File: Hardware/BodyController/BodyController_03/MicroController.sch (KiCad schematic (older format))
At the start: 17 parts, among them U1 PIC33EPxxxMU810, Y1 8MHz

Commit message: started serious layout
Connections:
- net FAN_SPEED_2_PWM is gone; now on net PUMP_SPEED_1_PWM: U1.88 (VCMPST2/RP97/RF1)
- net PUMP_SPEED_2_PWM is gone; now on net FAN_1_EN: U1.51 (USBID/RP99/RF3)
- net BATT_~FAULT: now also U1.19 (AN21/RPI89/RE9); no longer U1.5 (AN31/PWM4H/PMD7/RP87/RE7)
- net FAN_1_EN: no longer U1.53 (RP104/RF8)
- net IC_CONTROLLER_SLEEP: no longer U1.59 (ASDA2/RPI19/RA3)
- net IC_CONTROLLER_~FLT: now also U1.5 (AN31/PWM4H/PMD7/RP87/RE7); no longer U1.19 (AN21/RPI89/RE9)
- net PUMP_1_EN: now also U1.52 (RP98/RF2); no longer U1.49 (SDA2/PMA9/RP100/RF4)
- net PUMP_SPEED_1_PWM: no longer U1.52 (RP98/RF2)
- net BRAKE_SWITCH_2_IN: now reaches U1.40 (RP108/RF12)
- net TURN_RIGHT_SWITCH_IN: now reaches U1.56 (D-/RG3)
- net TURN_LEFT_SWITCH_IN: now reaches U1.57 (D+/RG2)
- net SPARE_SWITCH_1_IN: now reaches U1.7 (AN17/PWM5H/RPI50/RC2)
- net SPARE_SWITCH_2_IN: now reaches U1.8 (AN18/PWM6L/RPI51/RC3)
- net KILL_SWITCH_IN: now reaches U1.89 (RP113/RG1)
- net IGNITION_SWITCH_IN: now reaches U1.90 (RP112/RG0)
- net KICKSTAND_SWITCH_IN: now reaches U1.95 (RP126/RG14)
- net BRIGHTS_SWITCH_IN: now reaches U1.96 (RPI124/RG12)
- net HORN_SWITCH_IN: now reaches U1.97 (RP125/RG13)
- net 12P_MONITOR renamed 12P_MONITOR_AI
- net 12V_MONITOR renamed 12V_MONITOR_AI
- net AUX_PORT_ISENSE renamed AUX_PORT_ISENSE_AI
- net BATT_ISENSE renamed BATT_ISENSE_AI
- net DCDC_ISENSE renamed DCDC_ISENSE_AI
- net ECU_1_ISENSE renamed ECU_1_ISENSE_AI
- net ECU_2_ISENSE renamed ECU_2_ISENSE_AI
- net FAN_2_EN renamed BRAKE_SWITCH_1_IN
- net FAN_ISENSE renamed FAN_ISENSE_AI
- net HEADLIGHT_ISENSE renamed HEADLIGHT_ISENSE_AI
- net HEATER_ISENSE renamed HEATER_ISENSE_AI
- net HORN_ISENSE renamed HORN_ISENSE_AI
- net IC_CONTROLLER_ISENSE renamed IC_CONTROLLER_ISENSE_AI
- net LOCK_ISENSE renamed LOCK_ISENSE_AI
- net PUMP_2_EN renamed DAC_PWM_2
- net PUMP_ISENSE renamed THROTTLE_SIGNAL_MONITOR_AI
- net TAILLIGHT_ISENSE renamed TAILLIGHT_ISENSE_AI
- new net DAC_PWM_1: U1.49 (SDA2/PMA9/RP100/RF4)
- no-connect marks 1 -> 6
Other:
- moved on the sheet: C1, C2, C3, C37, C4, C5, C6, C61, C7, C8, C9, L1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

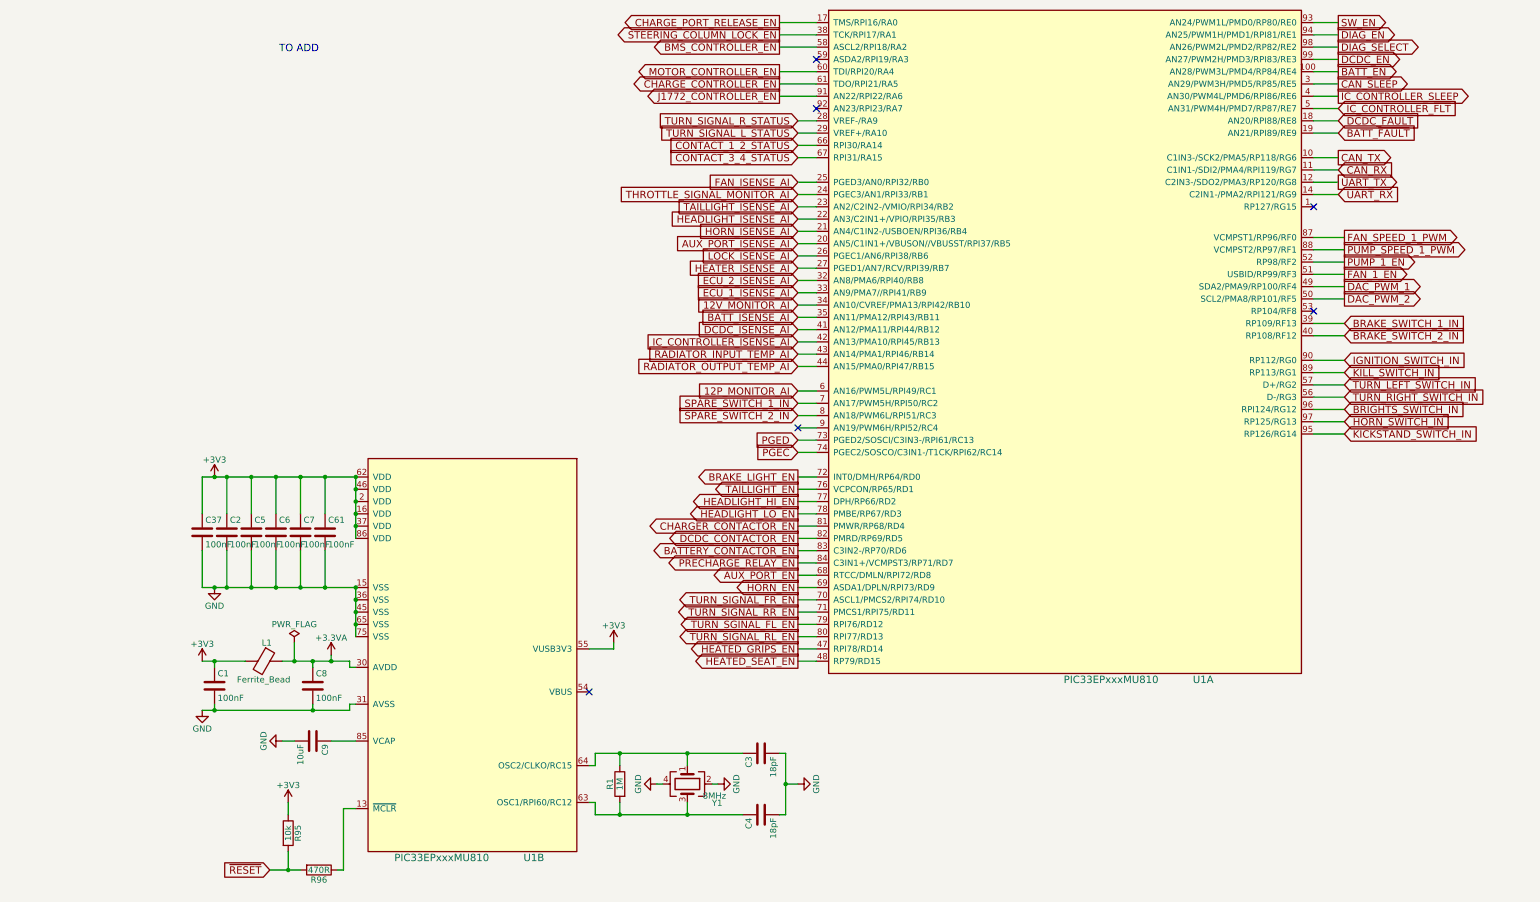
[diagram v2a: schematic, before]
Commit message: Body Controller Layout Done
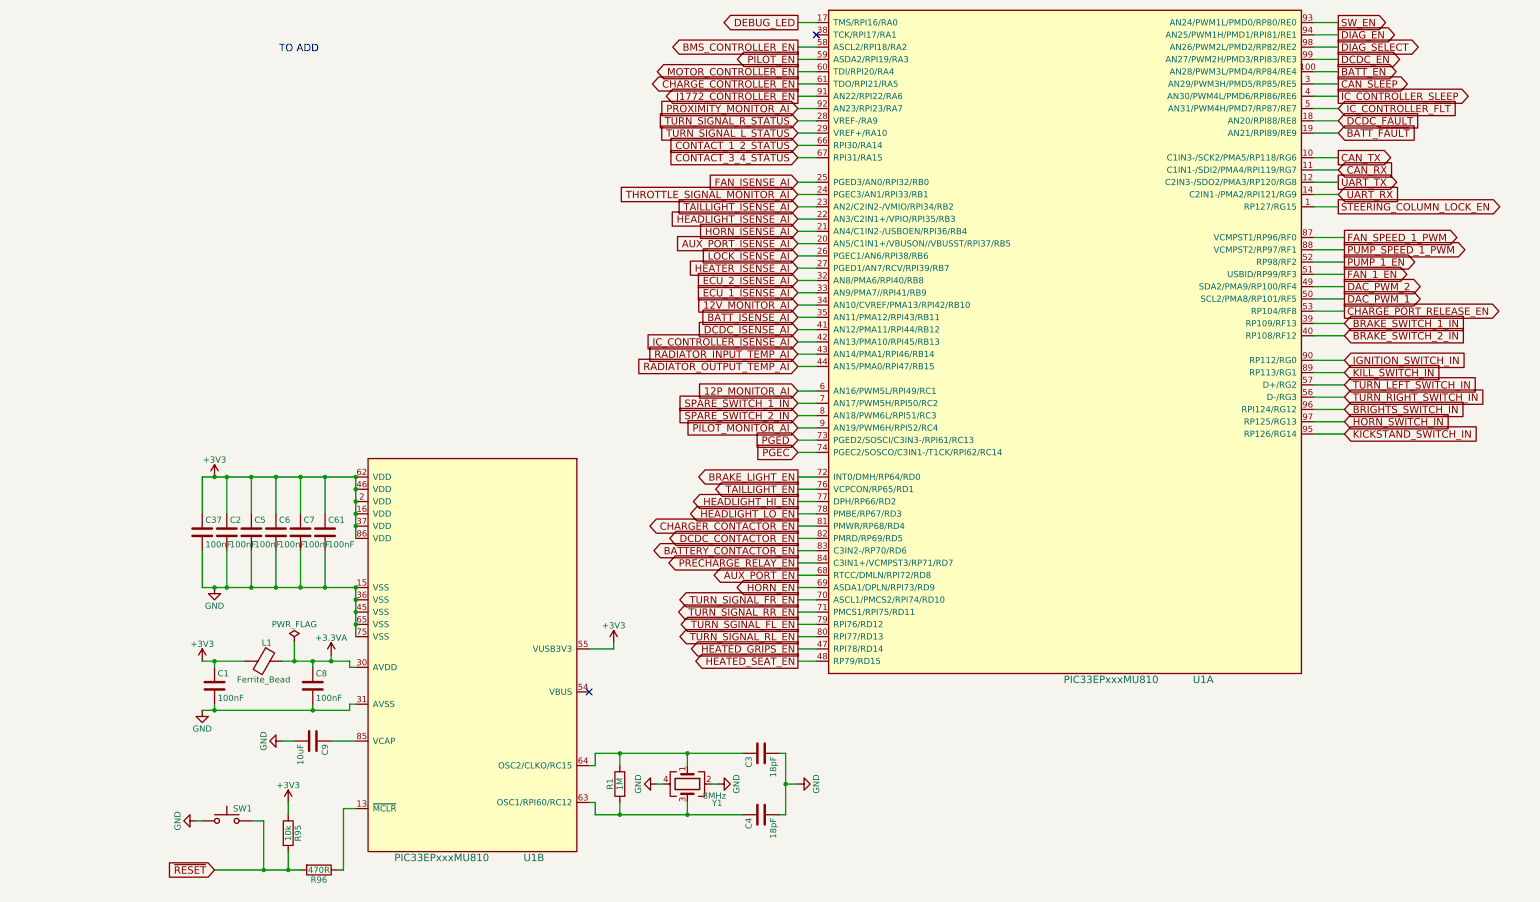
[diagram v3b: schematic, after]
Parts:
- added SW1: PTS645SM43SMTR92 LFS, Buttons_Switches_SMD:SW_SPST_EVQP0, symbol SW_Push
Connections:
- net CHARGE_PORT_RELEASE_EN: now also U1.53 (RP104/RF8); no longer U1.17 (TMS/RPI16/RA0)
- net DAC_PWM_1: now also U1.50 (SCL2/PMA8/RP101/RF5); no longer U1.49 (SDA2/PMA9/RP100/RF4)
- net DAC_PWM_2: now also U1.49 (SDA2/PMA9/RP100/RF4); no longer U1.50 (SCL2/PMA8/RP101/RF5)
- net GND: now also SW1.1
- net STEERING_COLUMN_LOCK_EN: now also U1.1 (RP127/RG15); no longer U1.38 (TCK/RPI17/RA1)
- net ~RESET: now also SW1.2
- net PILOT_EN: now reaches U1.59 (ASDA2/RPI19/RA3)
- net PILOT_MONITOR_AI: now reaches U1.9 (AN19/PWM6H/RPI52/RC4)
- net PROXIMITY_MONITOR_AI: now reaches U1.92 (AN23/RPI23/RA7)
- new net DEBUG_LED: U1.17 (TMS/RPI16/RA0)
- no-connect marks 6 -> 2
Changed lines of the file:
@@
 LIBS:ICs
 LIBS:Connectors
+LIBS:microchip_dspic33dsc
+LIBS:switches
 LIBS:BodyController_03-cache
 EELAYER 25 0
@@
 $Descr A4 11693 8268
 encoding utf-8
-Sheet 3 12
+Sheet 3 13
 Title ""
 Date ""
@@
 	1    4450 6900
 	0    1    -1   0
+$EndComp
+$Comp
+L GND #PWR013
+U 1 1 5A45E91E
+P 700 7200
+F 0 "#PWR013" H 700 6950 50  0001 C CNN
+F 1 "GND" H 700 7050 50  0000 C CNN
+F 2 "" H 700 7200 50  0001 C CNN
+F 3 "" H 700 7200 50  0001 C CNN
+	1    700  7200
+	0    1    1    0
+$EndComp
+$Comp
+L SW_Push SW1
+U 1 1 5A45E5E7
+P 950 7200
+F 0 "SW1" H 1000 7300 50  0000 L CNN
+F 1 "PTS645SM43SMTR92 LFS" H 950 7140 50  0001 C CNN
+F 2 "Buttons_Switches_SMD:SW_SPST_EVQP0" H 950 7400 50  0001 C CNN
+F 3 "https://www.ckswitches.com/media/1471/pts645.pdf" H 950 7400 50  0001 C CNN
+F 4 "PTS645SM43SMTR92 LFS" H 0   0   50  0001 C CNN "PartNumber"
+	1    950  7200
+	1    0    0    -1
 $EndComp
 Text GLabel 10000 700  2    59   Output ~ 0
@@
 Text GLabel 5600 3400 0    60   Input ~ 0
 RADIATOR_INPUT_TEMP_AI
-Text GLabel 5450 700  0    59   Output ~ 0
+Text GLabel 10050 3050 2    59   Output ~ 0
 CHARGE_PORT_RELEASE_EN
-Text GLabel 5450 800  0    59   Output ~ 0
+Text GLabel 10000 2200 2    59   Output ~ 0
 STEERING_COLUMN_LOCK_EN
 Text GLabel 5600 2600 0    59   Input ~ 0
@@
 Text GLabel 5600 1800 0    59   Input ~ 0
 CONTACT_3_4_STATUS
-Text GLabel 5450 1100 0    59   Output ~ 0
+Text GLabel 5600 1100 0    59   Output ~ 0
 MOTOR_CONTROLLER_EN
-Text GLabel 5450 1200 0    59   Output ~ 0
+Text GLabel 5600 1200 0    59   Output ~ 0
 CHARGE_CONTROLLER_EN
 Text GLabel 5600 2800 0    59   Input ~ 0
 ECU_2_ISENSE_AI
-Text GLabel 5450 900  0    59   Output ~ 0
+Text GLabel 5600 900  0    59   Output ~ 0
 BMS_CONTROLLER_EN
 Text GLabel 5600 2900 0    59   Input ~ 0
@@
 Text Notes 1700 950  2    60   ~ 0
 TO ADD
-Text GLabel 1300 7600 0    60   Input ~ 0
+Text GLabel 850  7600 0    60   Input ~ 0
 ~RESET
 Text GLabel 5600 4100 0    60   Input ~ 0
@@
 Text GLabel 10000 1300 2    59   Output ~ 0
 IC_CONTROLLER_SLEEP
-Text GLabel 5450 1300 0    59   Output ~ 0
+Text GLabel 5600 1300 0    59   Output ~ 0
 J1772_CONTROLLER_EN
 Text GLabel 10050 2450 2    60   Output ~ 0
@@
 Text GLabel 5600 3900 0    60   Input ~ 0
 SPARE_SWITCH_2_IN
+Text GLabel 5600 2100 0    60   Input ~ 0
+THROTTLE_SIGNAL_MONITOR_AI
+Text GLabel 10050 3150 2    60   Input ~ 0
+BRAKE_SWITCH_1_IN
+Text GLabel 10050 3250 2    60   Input ~ 0
+BRAKE_SWITCH_2_IN
+Text GLabel 10050 2950 2    60   Output ~ 0
+DAC_PWM_1
+Text GLabel 10050 2850 2    60   Output ~ 0
+DAC_PWM_2
+Text GLabel 5600 700  0    60   Output ~ 0
+DEBUG_LED
+Text GLabel 5600 4000 0    60   Input ~ 0
+PILOT_MONITOR_AI
+Text GLabel 5600 1400 0    60   Input ~ 0
+PROXIMITY_MONITOR_AI
+Text GLabel 5600 1000 0    60   Output ~ 0
+PILOT_EN
 Wire Wire Line
 	750  5300 2000 5300
@@
 	1450 7050 1450 7150
 Wire Wire Line
-	1450 7450 1450 7600
-Wire Wire Line
-	1300 7600 1550 7600
+	1450 7600 1450 7450
+Wire Wire Line
+	850  7600 1550 7600
 Wire Wire Line
 	1800 5850 1800 5900
@@
 	5600 1500 5750 1500
 Wire Wire Line
-	5750 1300 5450 1300
-Wire Wire Line
-	5450 1200 5750 1200
-Wire Wire Line
-	5750 1100 5450 1100
-Wire Wire Line
-	5750 900  5450 900
-Wire Wire Line
-	5450 800  5750 800
-Wire Wire Line
-	5750 700  5450 700
+	5750 1300 5600 1300
+Wire Wire Line
+	5600 1200 5750 1200
+Wire Wire Line
+	5750 1100 5600 1100
+Wire Wire Line
+	5750 900  5600 900
+Wire Wire Line
+	5750 700  5600 700
 Wire Wire Line
 	4100 5750 4100 5800
@@
 Wire Wire Line
 	5750 3900 5600 3900
+Wire Wire Line
+	5600 4000 5750 4000
+Wire Wire Line
+	10050 3250 9800 3250
+Wire Wire Line
+	10050 2950 9800 2950
+Wire Wire Line
+	9800 2850 10050 2850
+Wire Wire Line
+	5750 2100 5600 2100
+Wire Wire Line
+	9800 2200 10000 2200
+Wire Wire Line
+	1250 7600 1250 7200
+Wire Wire Line
+	750  7200 700  7200
+Wire Wire Line
+	1250 7200 1150 7200
+Wire Wire Line
+	10050 3050 9800 3050
+Wire Wire Line
+	5750 1400 5600 1400
+Wire Wire Line
+	5750 1000 5600 1000
 Connection ~ 950  4400
 Connection ~ 1150 4400
@@
 Connection ~ 5500 6900
 Connection ~ 2000 4400
+Connection ~ 1250 7600
 NoConn ~ 3900 6150
-Text GLabel 5600 2100 0    60   Input ~ 0
-THROTTLE_SIGNAL_MONITOR_AI
-Text GLabel 10050 3150 2    60   Input ~ 0
-BRAKE_SWITCH_1_IN
-Text GLabel 10050 3250 2    60   Input ~ 0
-BRAKE_SWITCH_2_IN
-Wire Wire Line
-	5600 4000 5750 4000
-Wire Wire Line
-	10050 3250 9800 3250
-NoConn ~ 9800 3050
-NoConn ~ 9800 2200
-NoConn ~ 5750 1000
-NoConn ~ 5750 1400
-Text GLabel 10050 2850 2    60   Output ~ 0
-DAC_PWM_1
-Text GLabel 10050 2950 2    60   Output ~ 0
-DAC_PWM_2
-Wire Wire Line
-	10050 2950 9800 2950
-Wire Wire Line
-	9800 2850 10050 2850
-Wire Wire Line
-	5750 2100 5600 2100
-NoConn ~ 5600 4000
+NoConn ~ 5750 800
 $EndSCHEMATC

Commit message: Added resistor values via BOM importer. Changed layout file to add large CAN resistors and buffer to 1.65V Reference
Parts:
- R1: PartNumber (none) -> AC0603FR-071ML
- R95: PartNumber (none) -> AC0603FR-0710KL
- R96: PartNumber (none) -> AC0603FR-07470RL
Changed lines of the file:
@@
 EESchema Schematic File Version 2
+LIBS:BodyController_03-rescue
 LIBS:power
 LIBS:device
@@
 $EndDescr
 $Comp
-L +3V3 #PWR4
+L +3V3 #PWR01
 U 1 1 59953D12
 P 850 4400
-F 0 "#PWR4" H 850 4250 50  0001 C CNN
+F 0 "#PWR01" H 850 4250 50  0001 C CNN
 F 1 "+3V3" H 850 4540 50  0000 C CNN
 F 2 "" H 850 4400 50  0001 C CNN
@@
 $EndComp
 $Comp
-L GND #PWR5
+L GND #PWR02
 U 1 1 59953D98
 P 850 5300
-F 0 "#PWR5" H 850 5050 50  0001 C CNN
+F 0 "#PWR02" H 850 5050 50  0001 C CNN
 F 1 "GND" H 850 5150 50  0000 C CNN
 F 2 "" H 850 5300 50  0001 C CNN
@@
 $EndComp
 $Comp
-L GND #PWR6
+L GND #PWR03
 U 1 1 5995450B
 P 1400 6550
-F 0 "#PWR6" H 1400 6300 50  0001 C CNN
+F 0 "#PWR03" H 1400 6300 50  0001 C CNN
 F 1 "GND" H 1400 6400 50  0000 C CNN
 F 2 "" H 1400 6550 50  0001 C CNN
@@
 $EndComp
 $Comp
-L +3V3 #PWR2
+L +3V3 #PWR04
 U 1 1 59955FA7
 P 750 5900
-F 0 "#PWR2" H 750 5750 50  0001 C CNN
+F 0 "#PWR04" H 750 5750 50  0001 C CNN
 F 1 "+3V3" H 750 6040 50  0000 C CNN
 F 2 "" H 750 5900 50  0001 C CNN
@@
 $EndComp
 $Comp
-L GND #PWR3
+L GND #PWR05
 U 1 1 59955FD3
 P 750 6300
-F 0 "#PWR3" H 750 6050 50  0001 C CNN
+F 0 "#PWR05" H 750 6050 50  0001 C CNN
 F 1 "GND" H 750 6150 50  0000 C CNN
 F 2 "" H 750 6300 50  0001 C CNN
@@
 F 1 "1M" V 4150 6900 50  0000 C CNN
 F 2 "Resistors_SMD:R_0603" V 4080 6900 50  0001 C CNN
-F 3 "" H 4150 6900 50  0001 C CNN
+F 3 "http://www.yageo.com/NewPortal/yageodocoutput?fileName=/pdf/R-Chip/PYu-AC_51_RoHS_L_6.pdf" H 4150 6900 50  0001 C CNN
+F 4 "AC0603FR-071ML" H 0   0   50  0001 C CNN "PartNumber"
 	1    4150 6900
 	-1   0    0    -1
 $EndComp
 $Comp
-L GND #PWR12
+L GND #PWR06
 U 1 1 5995664C
 P 5600 6900
-F 0 "#PWR12" H 5600 6650 50  0001 C CNN
+F 0 "#PWR06" H 5600 6650 50  0001 C CNN
 F 1 "GND" H 5600 6750 50  0000 C CNN
 F 2 "" H 5600 6900 50  0001 C CNN
@@
 $EndComp
 $Comp
-L +3V3 #PWR7
+L +3V3 #PWR07
 U 1 1 59967AA0
 P 1450 7050
-F 0 "#PWR7" H 1450 6900 50  0001 C CNN
+F 0 "#PWR07" H 1450 6900 50  0001 C CNN
 F 1 "+3V3" H 1450 7190 50  0000 C CNN
 F 2 "" H 1450 7050 50  0001 C CNN
@@
 F 1 "10k" V 1450 7300 50  0000 C CNN
 F 2 "Resistors_SMD:R_0603" V 1380 7300 50  0001 C CNN
-F 3 "" H 1450 7300 50  0001 C CNN
+F 3 "http://www.yageo.com/NewPortal/yageodocoutput?fileName=/pdf/R-Chip/PYu-AC_51_RoHS_L_6.pdf" H 1450 7300 50  0001 C CNN
+F 4 "AC0603FR-0710KL" H 0   0   50  0001 C CNN "PartNumber"
 	1    1450 7300
 	1    0    0    -1
@@
 F 1 "470R" V 1700 7600 50  0000 C CNN
 F 2 "Resistors_SMD:R_0603" V 1630 7600 50  0001 C CNN
-F 3 "" H 1700 7600 50  0001 C CNN
+F 3 "http://www.yageo.com/NewPortal/yageodocoutput?fileName=/pdf/R-Chip/PYu-AC_51_RoHS_L_6.pdf" H 1700 7600 50  0001 C CNN
+F 4 "AC0603FR-07470RL" H 0   0   50  0001 C CNN "PartNumber"
 	1    1700 7600
 	0    1    1    0
 $EndComp
 $Comp
-L +3.3VA #PWR8
+L +3.3VA #PWR08
 U 1 1 59977C27
 P 1800 5850
-F 0 "#PWR8" H 1800 5700 50  0001 C CNN
+F 0 "#PWR08" H 1800 5700 50  0001 C CNN
 F 1 "+3.3VA" H 1800 5990 50  0000 C CNN
 F 2 "" H 1800 5850 50  0001 C CNN
@@
 $EndComp
 $Comp
-L PWR_FLAG #FLG1
+L PWR_FLAG #FLG09
 U 1 1 59980D1B
 P 1500 5750
-F 0 "#FLG1" H 1500 5825 50  0001 C CNN
+F 0 "#FLG09" H 1500 5825 50  0001 C CNN
 F 1 "PWR_FLAG" H 1500 5900 50  0000 C CNN
 F 2 "" H 1500 5750 50  0001 C CNN
@@
 $EndComp
 $Comp
-L +3V3 #PWR9
+L +3V3 #PWR010
 U 1 1 59B2845D
 P 4100 5750
-F 0 "#PWR9" H 4100 5600 50  0001 C CNN
+F 0 "#PWR010" H 4100 5600 50  0001 C CNN
 F 1 "+3V3" H 4100 5890 50  0000 C CNN
 F 2 "" H 4100 5750 50  0001 C CNN
@@
 $EndComp
 $Comp
-L GND #PWR11
+L GND #PWR011
 U 1 1 59BBA3D3
 P 4950 6900
-F 0 "#PWR11" H 4950 6650 50  0001 C CNN
+F 0 "#PWR011" H 4950 6650 50  0001 C CNN
 F 1 "GND" H 4950 6750 50  0000 C CNN
 F 2 "" H 4950 6900 50  0001 C CNN
@@
 $EndComp
 $Comp
-L GND #PWR10
+L GND #PWR012
 U 1 1 59BBA417
 P 4450 6900
-F 0 "#PWR10" H 4450 6650 50  0001 C CNN
+F 0 "#PWR012" H 4450 6650 50  0001 C CNN
 F 1 "GND" H 4450 6750 50  0000 C CNN
 F 2 "" H 4450 6900 50  0001 C CNN
@@
 $EndComp
 $Comp
-L GND #PWR1
+L GND #PWR013
 U 1 1 5A45E91E
 P 700 7200
-F 0 "#PWR1" H 700 6950 50  0001 C CNN
+F 0 "#PWR013" H 700 6950 50  0001 C CNN
 F 1 "GND" H 700 7050 50  0000 C CNN
 F 2 "" H 700 7200 50  0001 C CNN
